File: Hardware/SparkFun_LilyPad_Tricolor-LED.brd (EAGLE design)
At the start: 20 x 20 mm, 11 parts

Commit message: revising to common cathode LED
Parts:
- removed D1: LED-TRICOLOR, SparkFun:LED-TRICOLOR-SMD
- added D2: XZM2CRKM2DGFBB45SCCB, SparkFun-LED:PLCC4SMDLED
- added FRAME1: FRAME-LETTER, SparkFun-Aesthetics:CREATIVE_COMMONS
- added LOGO1: REVISION, SparkFun-Aesthetics:REVISION
- added U$11: (no value), buzzard_labels (1):B2
- added U$12: (no value), buzzard_labels (1):G1
- added U$13: (no value), buzzard_labels (1):GND6
- added U$14: (no value), buzzard_labels (1):R0
- added U$4: (no value), buzzard_labels (1):95
- added U$5: (no value), buzzard_labels (1):104
- added U$6: (no value), buzzard_labels (1):113
- moved R1 14.4 mm to (6.26, 7.91)
- moved R2 14.4 mm to (10.2, 5.66)
- moved R3 14.4 mm to (14.1, 7.91)
- moved U$1 14.4 mm to (10.2, 10.2)
- moved U$2 14.4 mm to (16.7, 13.9)
- moved U$3 14.4 mm to (3.66, 13.9)
- moved U$7 14.4 mm to (3.66, 6.40)
- moved U$8 14.4 mm to (16.7, 6.40)
- moved U$9 14.4 mm to (10.2, 2.67)
- moved U$10 14.4 mm to (10.2, 17.7)
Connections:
- removed net +: D1.A, U$10.1
- new net -: D2.4, U$10.1
- net BLU: now also D2.3; no longer D1.B
- net GRN: now also D2.2; no longer D1.G
- net RED: now also D2.1; no longer D1.R
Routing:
- net -: track 0.00 -> 9.47 mm
- net +: track 6.41 -> 0.00 mm
- net RED: track 6.12 -> 3.99 mm
- net BLU: track 2.71 -> 3.78 mm
- net GRN: track 3.24 -> 4.07 mm
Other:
- board text removed: "+"
- board text removed: "10"
- board text removed: "11"
- board text removed: "9"
- board text removed: "B"
- board text removed: "G"
- board text removed: "R"

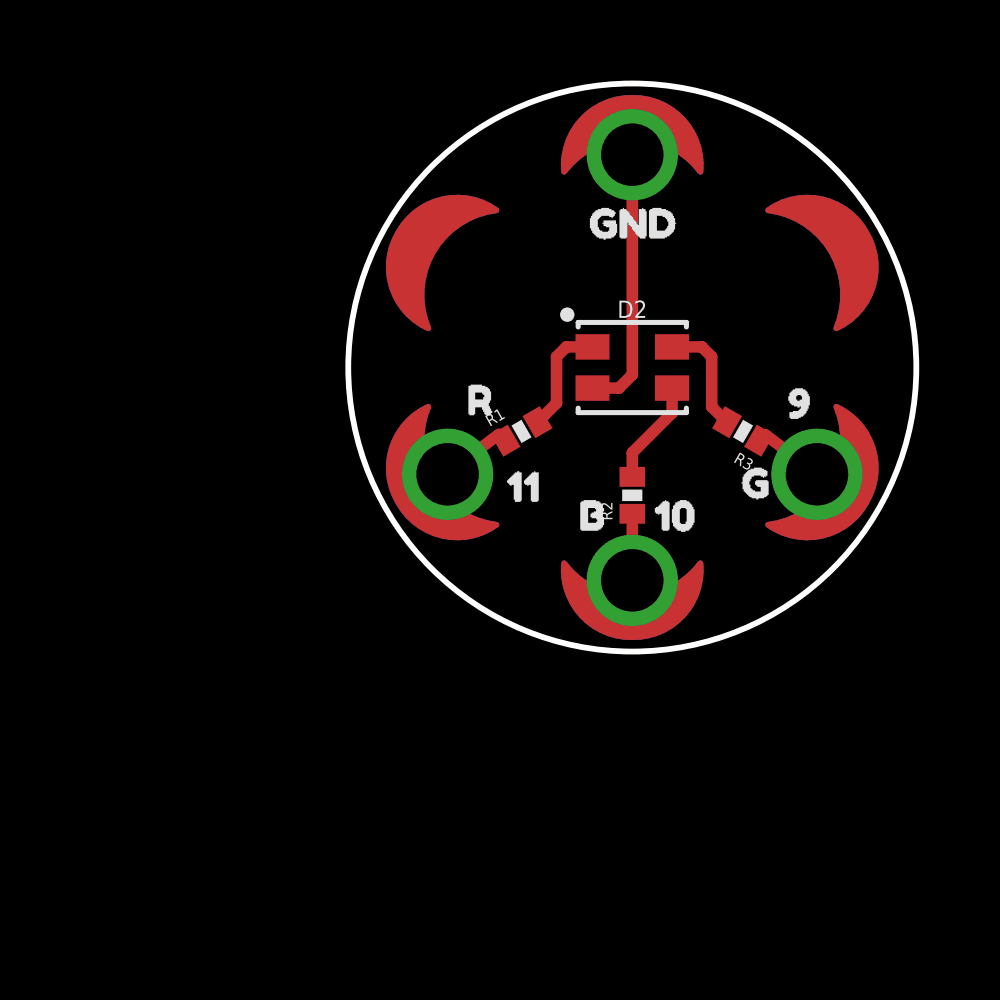
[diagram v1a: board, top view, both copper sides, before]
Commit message: revising to common cathode
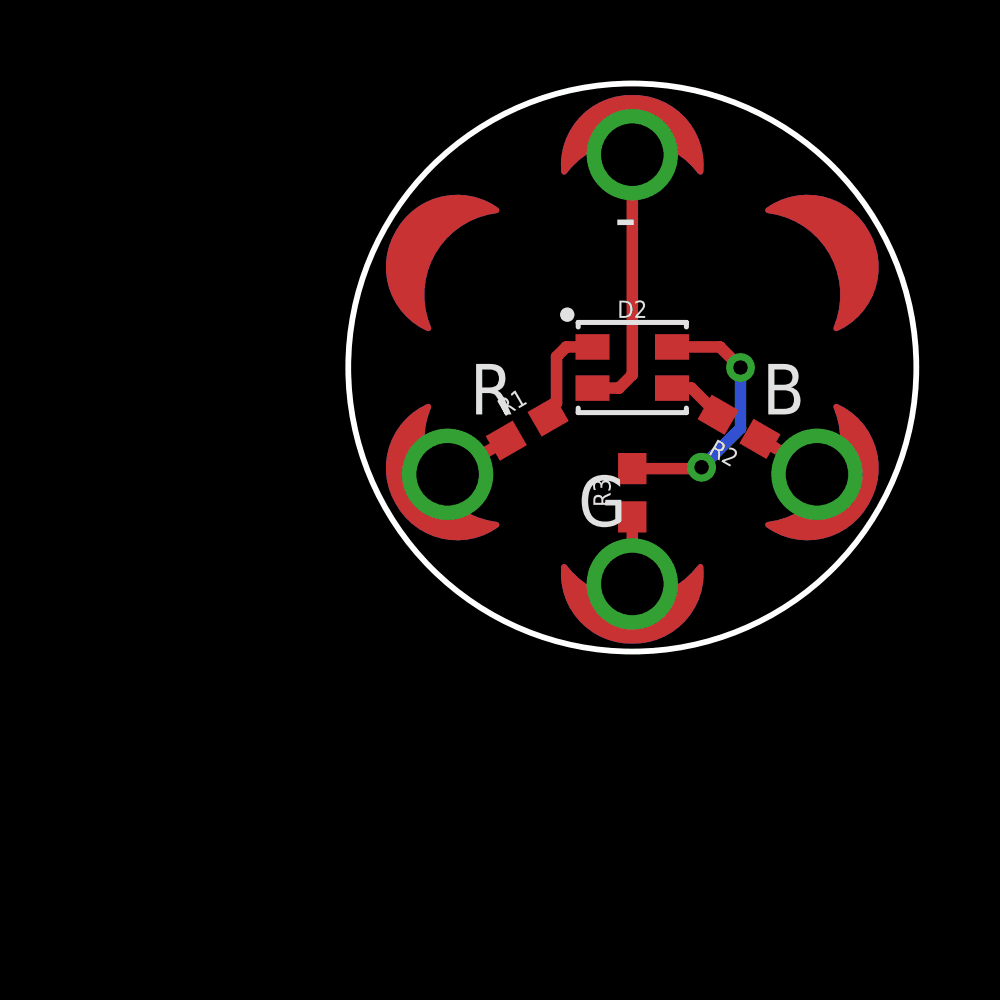
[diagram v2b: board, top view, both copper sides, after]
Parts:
- removed U$11: (no value), buzzard_labels (1):B2
- removed U$12: (no value), buzzard_labels (1):G1
- removed U$13: (no value), buzzard_labels (1):GND6
- removed U$14: (no value), buzzard_labels (1):R0
- removed U$4: (no value), buzzard_labels (1):95
- removed U$5: (no value), buzzard_labels (1):104
- removed U$6: (no value), buzzard_labels (1):113
- added LOGO2: OSHW-LOGOS, SparkFun-Aesthetics:OSHW-LOGO-S
- R1, R2, R3: device SparkFun:0402-RES -> SparkFun-Resistors:0603
- U$1: value LOGO-LPL -> LOGO-LPLP; device LilyPad-Wearables:LOGO-L -> SparkFun-Retired:LOGO-LILYPAD
- moved LOGO1 110.5 mm to (-7.62, -14.0)
- moved FRAME1 80.8 mm to (-18.9, -11.4)
- moved U$8 7.56 mm to (10.2, 2.54), turned to 0 degrees
- moved U$9 7.50 mm to (16.7, 6.40), turned to 60 degrees
- moved R2 4.47 mm to (13.9, 8.07), turned to 150 degrees
- moved R3 4.46 mm to (10.2, 5.75), turned to 90 degrees
- moved R1 0.22 mm to (6.46, 8.01)
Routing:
- net GRN: track 4.07 -> 9.25 mm, vias 0 -> 2
- net BLU: track 3.78 -> 2.01 mm
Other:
- board text added: "-"
- board text added: "B"
- board text added: "G"
- board text added: "R"
- board text added: "RGB LED"

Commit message: post design review changes
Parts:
- added U$4: (no value), SparkFun-Aesthetics:SFE_LOGO_FLAME_.1
- moved LOGO2 6.83 mm to (5.59, 12.7), flipped to the top
- moved R1 2.15 mm to (6.35, 10.2), turned to 0 degrees
- moved R2 2.09 mm to (14.0, 10.2), turned to 180 degrees
- moved R3 1.87 mm to (10.2, 7.62), turned to 0 degrees
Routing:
- net G: track 2.36 -> 5.43 mm
- net R: track 2.43 -> 4.55 mm
- net GRN: track 9.25 -> 11.3 mm
- net B: track 2.37 -> 4.20 mm
- net RED: track 3.64 -> 2.21 mm

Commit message: updating
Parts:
- removed U$4: (no value), SparkFun-Aesthetics:SFE_LOGO_FLAME_.1
- added FD1, FD2, FD3, FD4: FIDUCIAL1X2, SparkFun-Aesthetics:FIDUCIAL-1X2
- added LOGO3: SFE_LOGO_FLAME.1_INCH, SparkFun-Aesthetics:SFE_LOGO_FLAME_.1
- moved U$1 1.38 mm to (11.0, 11.3)
- moved LOGO2 1.19 mm to (6.44, 13.5)
- moved R1 1.19 mm to (7.20, 11.0)
- moved U$3 1.19 mm to (4.51, 14.8)
- moved D2 1.19 mm to (11.0, 11.0)
- moved R2 1.19 mm to (14.8, 11.0)
- moved U$10 1.19 mm to (11.0, 18.5)
- moved U$2 1.19 mm to (17.5, 14.8)
- moved U$7 1.19 mm to (4.51, 7.24)
- moved U$8 1.19 mm to (11.0, 3.38)
- moved R3 1.19 mm to (11.0, 8.46)
- moved U$9 1.19 mm to (17.5, 7.24)
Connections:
- net - renamed GND
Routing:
- net GRN: track 11.3 -> 12.2 mm
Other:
- board text added: "Andy England"
- board text added: "Dia Williams"
- board text added: "Units in MM"

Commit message: post review
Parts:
- added U$4: (no value), SparkFun-Aesthetics:ORDERING_INSTRUCTIONS
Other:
- board text added: "LilyPad Purple Soldermask"
- board text added: "Thin PCB - .8mm"
- board text added: "v20"
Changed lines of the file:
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@@
 <text x="11.6459" y="15.4432" size="1.778" layer="22" font="vector" ratio="15" rot="MR0">-</text>
 <dimension x1="3.254725" y1="4.686165625" x2="18.767075" y2="17.310234375" x3="2.56625625" y3="21.37490625" textsize="1.778" layer="47" dtype="diameter"/>
-<text x="5.08" y="-2.54" size="1.778" layer="47" font="vector">Units in MM</text>
+<text x="2.54" y="-2.54" size="1.778" layer="47" font="vector">Units in MM</text>
 <text x="11.43" y="-11.43" size="1.778" layer="51" font="vector">Dia Williams</text>
 <text x="10.16" y="-13.97" size="1.778" layer="51" font="vector">Andy England</text>
+<text x="-7.62" y="-27.94" size="1.778" layer="51" font="vector">Thin PCB - .8mm</text>
+<text x="-7.62" y="-31.75" size="1.778" layer="51" font="vector">LilyPad Purple Soldermask</text>
+<text x="4.0513" y="12.2047" size="1.016" layer="16" font="vector" ratio="15" rot="MR90">v20</text>
 </plain>
 <attributes>
@@
 <element name="FD3" library="SparkFun-Aesthetics" package="FIDUCIAL-1X2" value="FIDUCIAL1X2" x="15.24" y="17.78"/>
 <element name="FD4" library="SparkFun-Aesthetics" package="FIDUCIAL-1X2" value="FIDUCIAL1X2" x="15.24" y="17.78" rot="MR0"/>
+<element name="U$4" library="SparkFun-Aesthetics" package="ORDERING_INSTRUCTIONS" value="" x="-10.16" y="-15.24"/>
 </elements>
 <signals>
